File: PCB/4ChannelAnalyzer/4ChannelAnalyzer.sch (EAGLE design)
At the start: 18 parts, among them U1 ADS1015IDGST, U2 ADS1015IDGST, X3 MINI-USB-32005-301

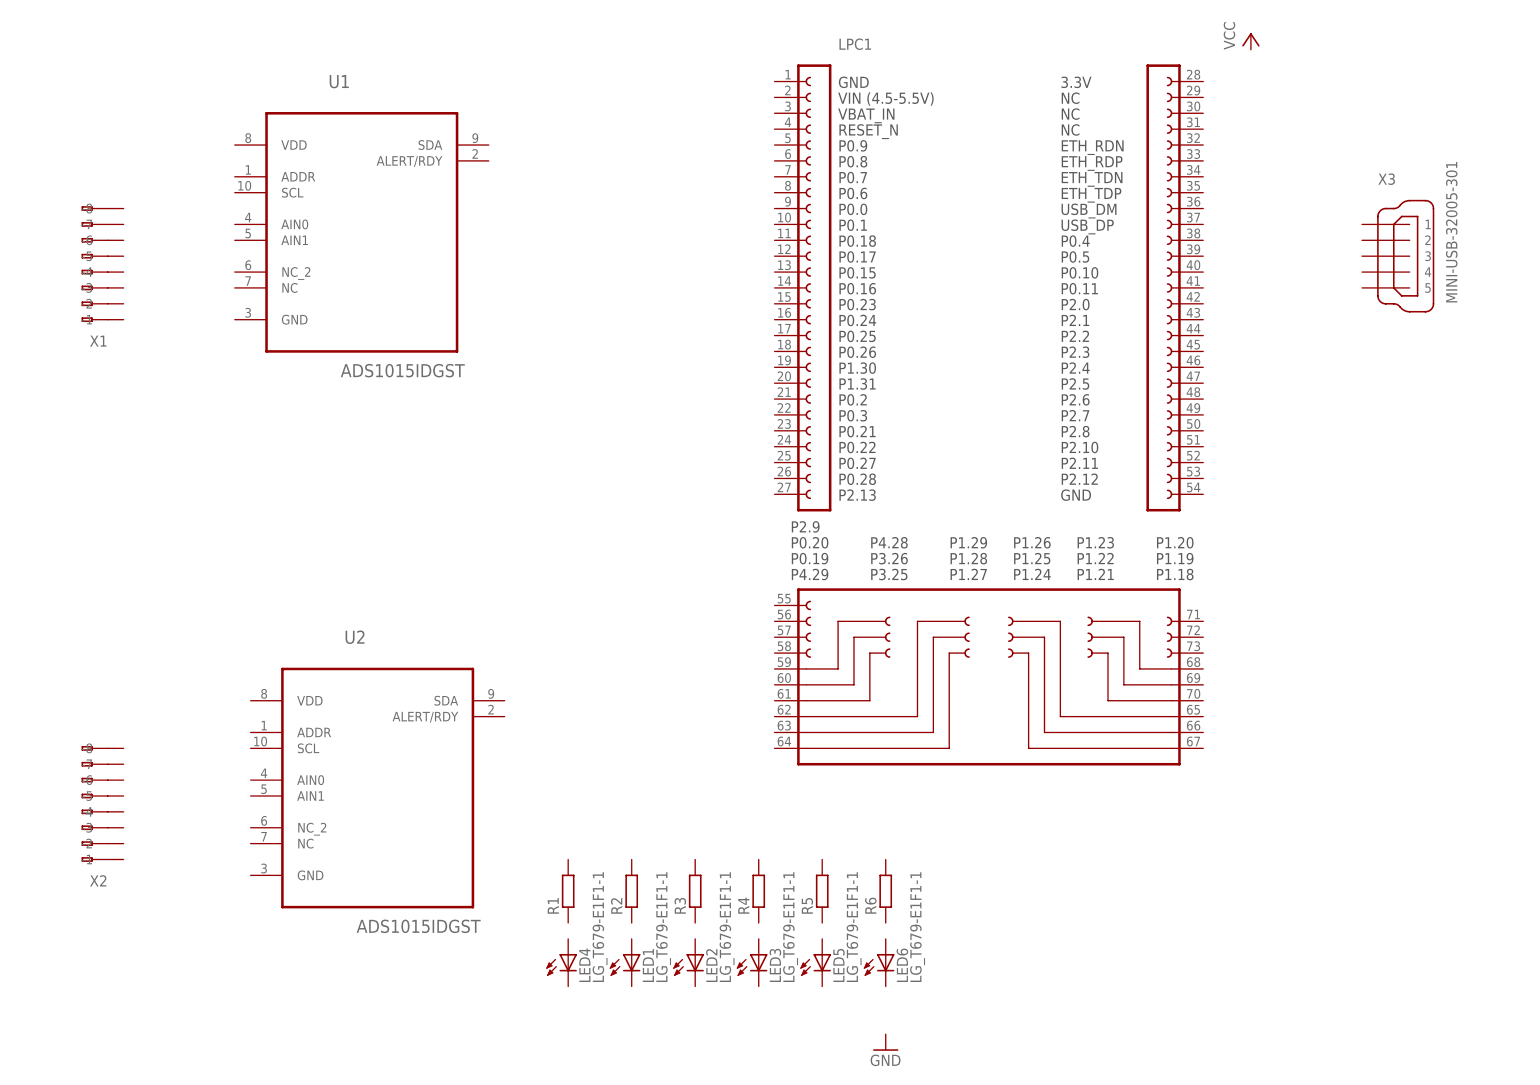
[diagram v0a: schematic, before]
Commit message: Wiring ADCs with connectors and LED.
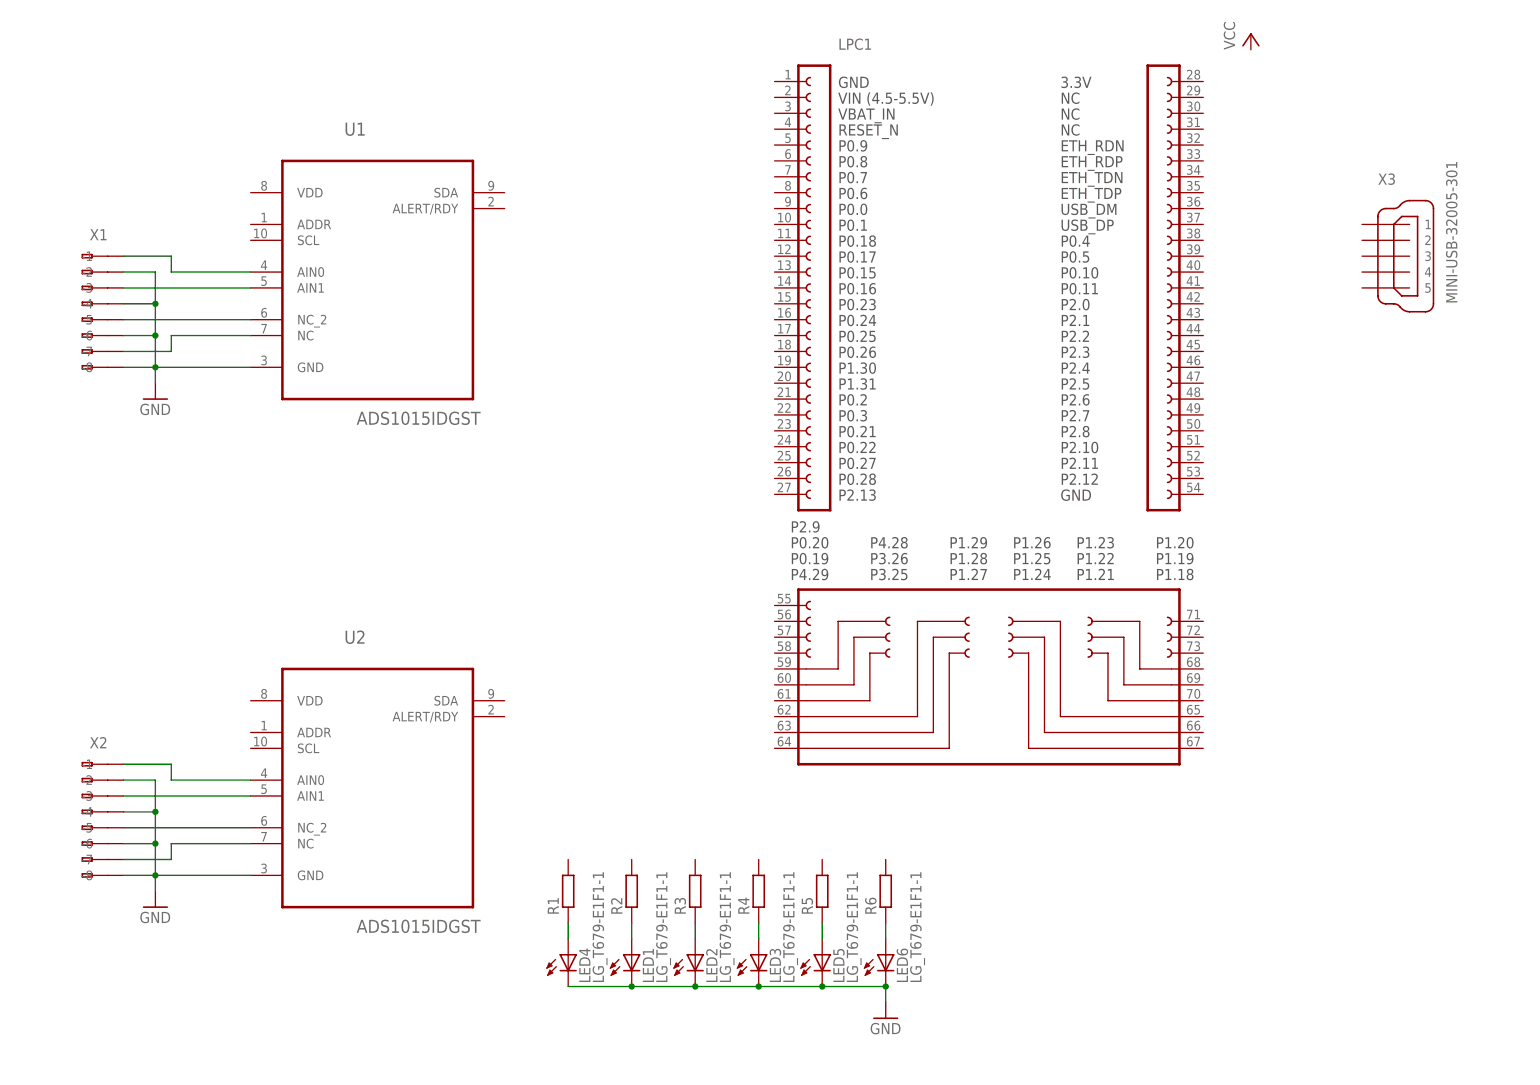
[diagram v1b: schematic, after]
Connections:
- new net GND: LED1.C, LED2.C, LED3.C, LED4.C, LED5.C, LED6.C, U1.GND, U2.GND, X1.-2, X1.-4, X1.-6, X1.-8, X2.-2, X2.-4, X2.-6, X2.-8
- new net N$1: U1.AIN0, X1.-1
- new net N$10: U2.AIN1, X2.-3
- new net N$11: U2.NC_2, X2.-5
- new net N$12: U2.NC, X2.-7
- new net N$13: U1.NC_2, X1.-5
- new net N$14: U1.NC, X1.-7
- new net N$2: LED4.A, R1.1
- new net N$3: LED1.A, R2.1
- new net N$4: LED2.A, R3.1
- new net N$5: LED3.A, R4.1
- new net N$6: LED5.A, R5.1
- new net N$7: LED6.A, R6.1
- new net N$8: U1.AIN1, X1.-3
- new net N$9: U2.AIN0, X2.-1
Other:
- moved on the sheet: U1, X1, X2
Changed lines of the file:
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@@
 <part name="FRAME1" library="frames" deviceset="A4L-LOC" device=""/>
 <part name="LPC1" library="LPCXpresso_LPC1769" deviceset="LPCXPRESSO_LPC1769" device=""/>
-<part name="U1" library="ADS1015" deviceset="ADS1015IDGST" device=""/>
 <part name="U2" library="ADS1015" deviceset="ADS1015IDGST" device=""/>
-<part name="X1" library="con-wago255" deviceset="233-108" device=""/>
 <part name="X2" library="con-wago255" deviceset="233-108" device=""/>
 <part name="X3" library="con-cypressindustries" deviceset="MINI-USB-" device="32005-301"/>
@@
 <part name="GND1" library="supply1" deviceset="GND" device=""/>
 <part name="P+1" library="supply1" deviceset="VCC" device=""/>
+<part name="GND2" library="supply1" deviceset="GND" device=""/>
+<part name="U1" library="ADS1015" deviceset="ADS1015IDGST" device=""/>
+<part name="X1" library="con-wago255" deviceset="233-108" device=""/>
+<part name="GND3" library="supply1" deviceset="GND" device=""/>
 </parts>
 <sheets>
@@
 <instance part="FRAME1" gate="G$1" x="0" y="0"/>
 <instance part="LPC1" gate="G$1" x="165.1" y="127"/>
-<instance part="U1" gate="A" x="68.58" y="142.24"/>
 <instance part="U2" gate="A" x="71.12" y="53.34"/>
-<instance part="X1" gate="G$1" x="22.86" y="132.08" rot="R180"/>
-<instance part="X2" gate="G$1" x="22.86" y="45.72" rot="R180"/>
+<instance part="X2" gate="G$1" x="22.86" y="45.72" rot="MR0"/>
 <instance part="X3" gate="G$1" x="233.68" y="134.62"/>
 <instance part="LED1" gate="G$1" x="111.76" y="22.86"/>
@@
 <instance part="R5" gate="G$1" x="142.24" y="33.02" rot="R90"/>
 <instance part="R6" gate="G$1" x="152.4" y="33.02" rot="R90"/>
-<instance part="GND1" gate="1" x="152.4" y="7.62"/>
+<instance part="GND1" gate="1" x="152.4" y="12.7"/>
 <instance part="P+1" gate="VCC" x="210.82" y="170.18"/>
+<instance part="GND2" gate="1" x="35.56" y="30.48"/>
+<instance part="U1" gate="A" x="71.12" y="134.62"/>
+<instance part="X1" gate="G$1" x="22.86" y="127" rot="MR0"/>
+<instance part="GND3" gate="1" x="35.56" y="111.76"/>
 </instances>
 <busses>
 </busses>
 <nets>
+<net name="GND" class="0">
+<segment>
+<pinref part="LED4" gate="G$1" pin="C"/>
+<pinref part="LED6" gate="G$1" pin="C"/>
+<wire x1="101.6" y1="17.78" x2="111.76" y2="17.78" width="0.1524" layer="91"/>
+<pinref part="GND1" gate="1" pin="GND"/>
+<wire x1="111.76" y1="17.78" x2="121.92" y2="17.78" width="0.1524" layer="91"/>
+<wire x1="121.92" y1="17.78" x2="132.08" y2="17.78" width="0.1524" layer="91"/>
+<wire x1="132.08" y1="17.78" x2="142.24" y2="17.78" width="0.1524" layer="91"/>
+<wire x1="142.24" y1="17.78" x2="152.4" y2="17.78" width="0.1524" layer="91"/>
+<wire x1="152.4" y1="17.78" x2="152.4" y2="15.24" width="0.1524" layer="91"/>
+<junction x="152.4" y="17.78"/>
+<pinref part="LED5" gate="G$1" pin="C"/>
+<junction x="142.24" y="17.78"/>
+<pinref part="LED3" gate="G$1" pin="C"/>
+<junction x="132.08" y="17.78"/>
+<pinref part="LED2" gate="G$1" pin="C"/>
+<junction x="121.92" y="17.78"/>
+<pinref part="LED1" gate="G$1" pin="C"/>
+<junction x="111.76" y="17.78"/>
+</segment>
+<segment>
+<pinref part="U2" gate="A" pin="GND"/>
+<pinref part="X2" gate="G$1" pin="-8"/>
+<wire x1="50.8" y1="35.56" x2="35.56" y2="35.56" width="0.1524" layer="91"/>
+<wire x1="35.56" y1="35.56" x2="30.48" y2="35.56" width="0.1524" layer="91"/>
+<pinref part="X2" gate="G$1" pin="-6"/>
+<wire x1="30.48" y1="40.64" x2="35.56" y2="40.64" width="0.1524" layer="91"/>
+<wire x1="35.56" y1="40.64" x2="35.56" y2="35.56" width="0.1524" layer="91"/>
+<pinref part="X2" gate="G$1" pin="-4"/>
+<wire x1="30.48" y1="45.72" x2="35.56" y2="45.72" width="0.1524" layer="91"/>
+<wire x1="35.56" y1="45.72" x2="35.56" y2="40.64" width="0.1524" layer="91"/>
+<pinref part="X2" gate="G$1" pin="-2"/>
+<wire x1="30.48" y1="50.8" x2="35.56" y2="50.8" width="0.1524" layer="91"/>
+<wire x1="35.56" y1="50.8" x2="35.56" y2="45.72" width="0.1524" layer="91"/>
+<junction x="35.56" y="40.64"/>
+<junction x="35.56" y="45.72"/>
+<junction x="35.56" y="35.56"/>
+<pinref part="GND2" gate="1" pin="GND"/>
+<wire x1="35.56" y1="33.02" x2="35.56" y2="35.56" width="0.1524" layer="91"/>
+</segment>
+<segment>
+<pinref part="U1" gate="A" pin="GND"/>
+<pinref part="X1" gate="G$1" pin="-8"/>
+<wire x1="50.8" y1="116.84" x2="35.56" y2="116.84" width="0.1524" layer="91"/>
+<wire x1="35.56" y1="116.84" x2="30.48" y2="116.84" width="0.1524" layer="91"/>
+<pinref part="X1" gate="G$1" pin="-6"/>
+<wire x1="30.48" y1="121.92" x2="35.56" y2="121.92" width="0.1524" layer="91"/>
+<wire x1="35.56" y1="121.92" x2="35.56" y2="116.84" width="0.1524" layer="91"/>
+<pinref part="X1" gate="G$1" pin="-4"/>
+<wire x1="30.48" y1="127" x2="35.56" y2="127" width="0.1524" layer="91"/>
+<wire x1="35.56" y1="127" x2="35.56" y2="121.92" width="0.1524" layer="91"/>
+<pinref part="X1" gate="G$1" pin="-2"/>
+<wire x1="30.48" y1="132.08" x2="35.56" y2="132.08" width="0.1524" layer="91"/>
+<wire x1="35.56" y1="132.08" x2="35.56" y2="127" width="0.1524" layer="91"/>
+<junction x="35.56" y="121.92"/>
+<junction x="35.56" y="127"/>
+<junction x="35.56" y="116.84"/>
+<pinref part="GND3" gate="1" pin="GND"/>
+<wire x1="35.56" y1="114.3" x2="35.56" y2="116.84" width="0.1524" layer="91"/>
+</segment>
+</net>
+<net name="N$2" class="0">
+<segment>
+<pinref part="R1" gate="G$1" pin="1"/>
+<pinref part="LED4" gate="G$1" pin="A"/>
+<wire x1="101.6" y1="27.94" x2="101.6" y2="25.4" width="0.1524" layer="91"/>
+</segment>
+</net>
+<net name="N$3" class="0">
+<segment>
+<pinref part="R2" gate="G$1" pin="1"/>
+<pinref part="LED1" gate="G$1" pin="A"/>
+<wire x1="111.76" y1="27.94" x2="111.76" y2="25.4" width="0.1524" layer="91"/>
+</segment>
+</net>
+<net name="N$4" class="0">
+<segment>
+<pinref part="R3" gate="G$1" pin="1"/>
+<pinref part="LED2" gate="G$1" pin="A"/>
+<wire x1="121.92" y1="27.94" x2="121.92" y2="25.4" width="0.1524" layer="91"/>
+</segment>
+</net>
+<net name="N$5" class="0">
+<segment>
+<pinref part="R4" gate="G$1" pin="1"/>
+<pinref part="LED3" gate="G$1" pin="A"/>
+<wire x1="132.08" y1="27.94" x2="132.08" y2="25.4" width="0.1524" layer="91"/>
+</segment>
+</net>
+<net name="N$6" class="0">
+<segment>
+<pinref part="R5" gate="G$1" pin="1"/>
+<pinref part="LED5" gate="G$1" pin="A"/>
+<wire x1="142.24" y1="27.94" x2="142.24" y2="25.4" width="0.1524" layer="91"/>
+</segment>
+</net>
+<net name="N$7" class="0">
+<segment>
+<pinref part="R6" gate="G$1" pin="1"/>
+<pinref part="LED6" gate="G$1" pin="A"/>
+<wire x1="152.4" y1="27.94" x2="152.4" y2="25.4" width="0.1524" layer="91"/>
+</segment>
+</net>
+<net name="N$9" class="0">
+<segment>
+<pinref part="U2" gate="A" pin="AIN0"/>
+<wire x1="50.8" y1="50.8" x2="38.1" y2="50.8" width="0.1524" layer="91"/>
+<wire x1="38.1" y1="50.8" x2="38.1" y2="53.34" width="0.1524" layer="91"/>
+<pinref part="X2" gate="G$1" pin="-1"/>
+<wire x1="38.1" y1="53.34" x2="30.48" y2="53.34" width="0.1524" layer="91"/>
+</segment>
+</net>
+<net name="N$10" class="0">
+<segment>
+<pinref part="U2" gate="A" pin="AIN1"/>
+<pinref part="X2" gate="G$1" pin="-3"/>
+<wire x1="50.8" y1="48.26" x2="30.48" y2="48.26" width="0.1524" layer="91"/>
+</segment>
+</net>
+<net name="N$11" class="0">
+<segment>
+<pinref part="U2" gate="A" pin="NC_2"/>
+<pinref part="X2" gate="G$1" pin="-5"/>
+<wire x1="50.8" y1="43.18" x2="30.48" y2="43.18" width="0.1524" layer="91"/>
+</segment>
+</net>
+<net name="N$12" class="0">
+<segment>
+<pinref part="U2" gate="A" pin="NC"/>
+<wire x1="50.8" y1="40.64" x2="38.1" y2="40.64" width="0.1524" layer="91"/>
+<wire x1="38.1" y1="40.64" x2="38.1" y2="38.1" width="0.1524" layer="91"/>
+<pinref part="X2" gate="G$1" pin="-7"/>
+<wire x1="38.1" y1="38.1" x2="30.48" y2="38.1" width="0.1524" layer="91"/>
+</segment>
+</net>
+<net name="N$1" class="0">
+<segment>
+<pinref part="U1" gate="A" pin="AIN0"/>
+<wire x1="50.8" y1="132.08" x2="38.1" y2="132.08" width="0.1524" layer="91"/>
+<wire x1="38.1" y1="132.08" x2="38.1" y2="134.62" width="0.1524" layer="91"/>
+<pinref part="X1" gate="G$1" pin="-1"/>
+<wire x1="38.1" y1="134.62" x2="30.48" y2="134.62" width="0.1524" layer="91"/>
+</segment>
+</net>
+<net name="N$8" class="0">
+<segment>
+<pinref part="U1" gate="A" pin="AIN1"/>
+<pinref part="X1" gate="G$1" pin="-3"/>
+<wire x1="50.8" y1="129.54" x2="30.48" y2="129.54" width="0.1524" layer="91"/>
+</segment>
+</net>
+<net name="N$13" class="0">
+<segment>
+<pinref part="U1" gate="A" pin="NC_2"/>
+<pinref part="X1" gate="G$1" pin="-5"/>
+<wire x1="50.8" y1="124.46" x2="30.48" y2="124.46" width="0.1524" layer="91"/>
+</segment>
+</net>
+<net name="N$14" class="0">
+<segment>
+<pinref part="U1" gate="A" pin="NC"/>
+<wire x1="50.8" y1="121.92" x2="38.1" y2="121.92" width="0.1524" layer="91"/>
+<wire x1="38.1" y1="121.92" x2="38.1" y2="119.38" width="0.1524" layer="91"/>
+<pinref part="X1" gate="G$1" pin="-7"/>
+<wire x1="38.1" y1="119.38" x2="30.48" y2="119.38" width="0.1524" layer="91"/>
+</segment>
+</net>
 </nets>
 </sheet>

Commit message: Added LM1117 Linear Voltage Stabilizer
Added LM1117 Linear Voltage Stabilizer
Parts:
- added U3: LM1117MP-3.3, LM1117MP-3.3:LM1117MP-3.3
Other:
- moved on the sheet: LPC1, X3
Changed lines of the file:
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@@
 <part name="X1" library="con-wago255" deviceset="233-108" device=""/>
 <part name="GND3" library="supply1" deviceset="GND" device=""/>
+<part name="U3" library="LM1117MP-3.3" deviceset="LM1117MP-3.3" device=""/>
 </parts>
 <sheets>
@@
 <instances>
 <instance part="FRAME1" gate="G$1" x="0" y="0"/>
-<instance part="LPC1" gate="G$1" x="165.1" y="127"/>
+<instance part="LPC1" gate="G$1" x="180.34" y="121.92"/>
 <instance part="U2" gate="A" x="71.12" y="53.34"/>
 <instance part="X2" gate="G$1" x="22.86" y="45.72" rot="MR0"/>
-<instance part="X3" gate="G$1" x="233.68" y="134.62"/>
+<instance part="X3" gate="G$1" x="233.68" y="149.86"/>
 <instance part="LED1" gate="G$1" x="111.76" y="22.86"/>
 <instance part="LED2" gate="G$1" x="121.92" y="22.86"/>
@@
 <instance part="R6" gate="G$1" x="152.4" y="33.02" rot="R90"/>
 <instance part="GND1" gate="1" x="152.4" y="12.7"/>
-<instance part="P+1" gate="VCC" x="210.82" y="170.18"/>
+<instance part="P+1" gate="VCC" x="220.98" y="167.64"/>
 <instance part="GND2" gate="1" x="35.56" y="30.48"/>
 <instance part="U1" gate="A" x="71.12" y="134.62"/>
 <instance part="X1" gate="G$1" x="22.86" y="127" rot="MR0"/>
 <instance part="GND3" gate="1" x="35.56" y="111.76"/>
+<instance part="U3" gate="A" x="111.76" y="88.9"/>
 </instances>
 <busses>
